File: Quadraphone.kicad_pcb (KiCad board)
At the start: 4 copper layers, 60 x 100 mm, 197 parts, among them J1 Conn_01x10_Male, J2 Conn_01x10_Male, J3 Conn_01x10_Male, J4 Conn_01x10_Male, J5 Eurorack_10_pin_power, Q1 MMBT3904, U1 AMS1117-5.0, U10 TL072, U11 74LV4066PW, U12 SSI2131, U13 TL072, U14 LM4040DBZ-2.5, U15 74LV4066PW, U16 TL072, U17 SSI2131, U18 TL072, U22 SSI2131, U3 MCP6002, U4 LM4040DBZ-5, U5 MCP6004, U6 74LV4066PW, U7 74LV4066PW, U8 74LV4066PW, U9 SSI2131

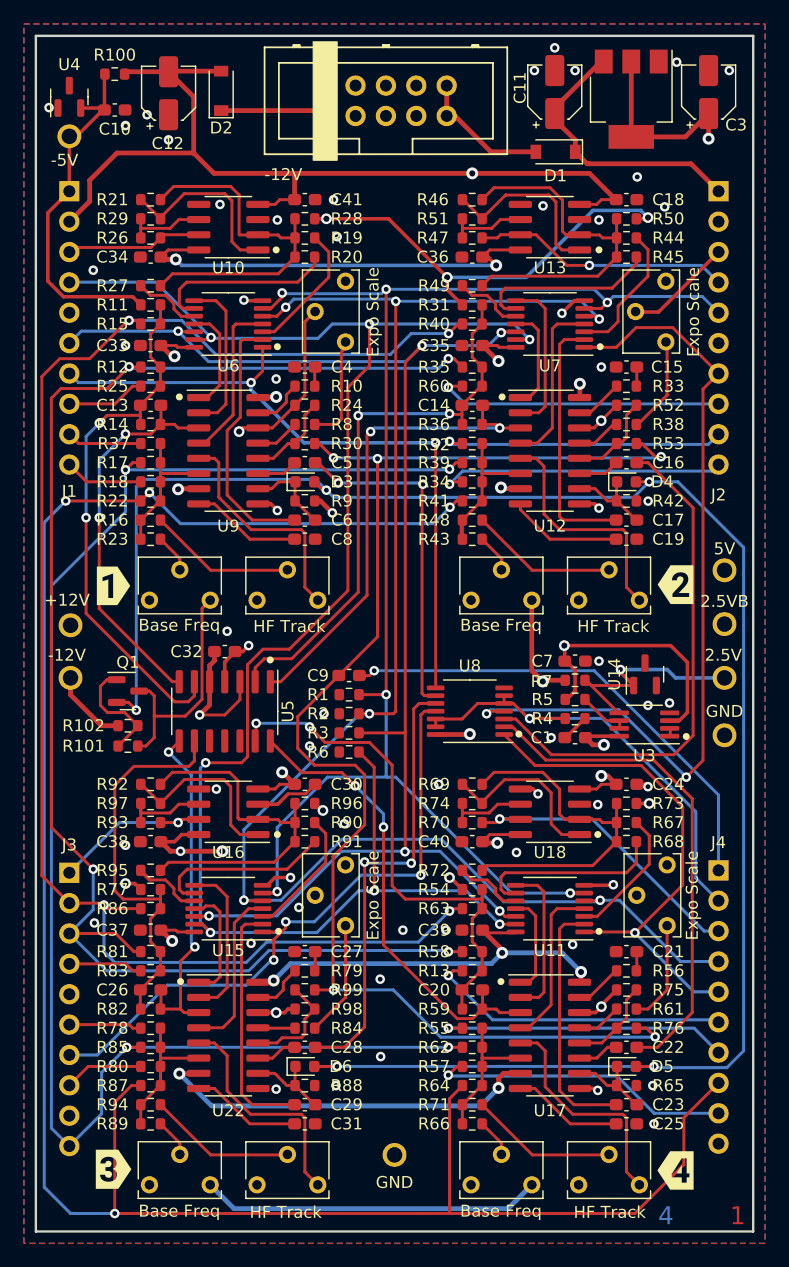
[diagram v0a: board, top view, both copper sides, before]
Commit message: Started Rev 3 with buffered octave control
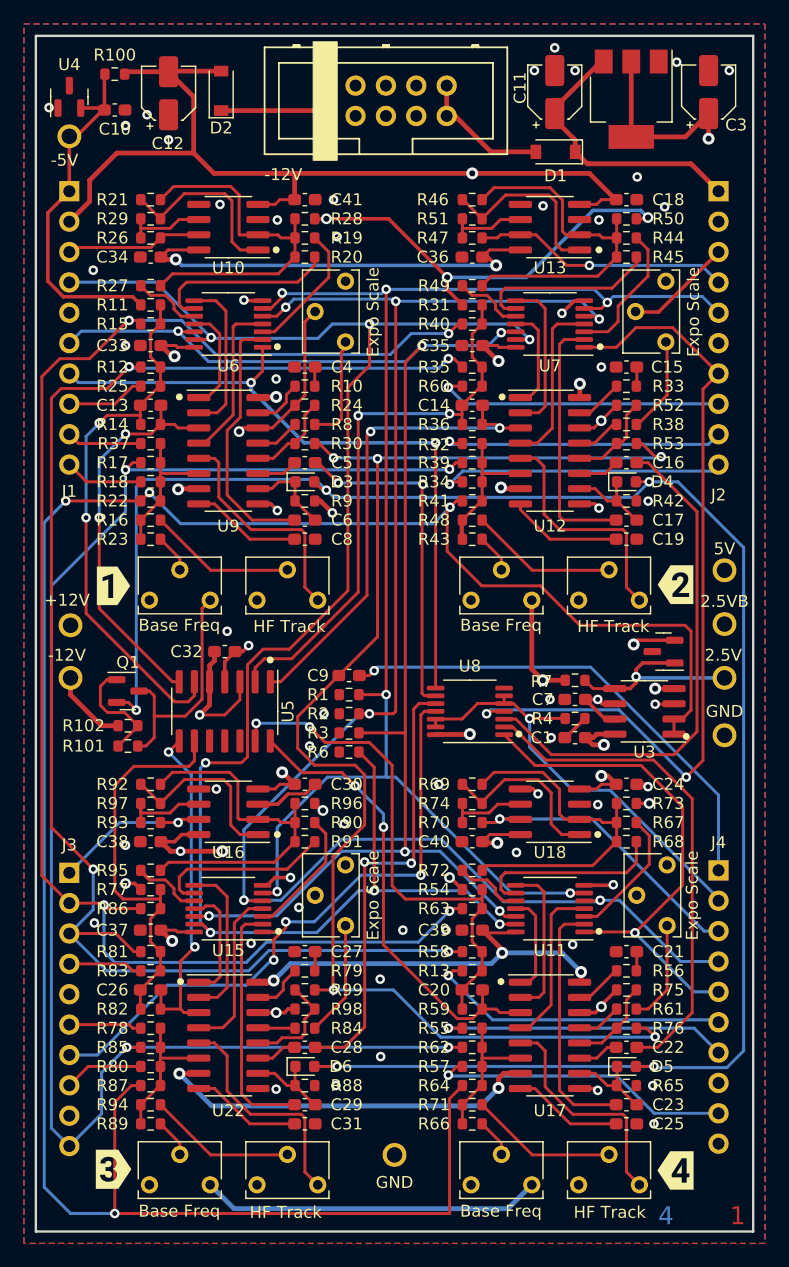
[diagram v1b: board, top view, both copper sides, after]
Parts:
- removed R5: 100, Resistor_SMD:R_0603_1608Metric
- U3: footprint Package_SO:MSOP-8_3x3mm_P0.65mm -> Package_SO:SOIC-8_3.9x4.9mm_P1.27mm
- moved C7 3.20 mm to (95.1, 105.5), turned to 0 degrees
- moved U14 2.45 mm to (102.5, 101.5), turned to 180 degrees
- moved U3 1.10 mm to (100.9, 106.5)
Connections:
- R22 pad 1: /OCT_TUNE -> /Oct_Buff
- R41 pad 1: /OCT_TUNE -> /Oct_Buff
- R64 pad 1: /OCT_TUNE -> /Oct_Buff
- R87 pad 1: /OCT_TUNE -> /Oct_Buff
- U3 pad 1: Net-(U3-Pad1) -> /Oct_Buff
- U3 pad 2: Net-(U3-Pad1) -> /Oct_Buff
- U3 pad 3: +2V5 -> /OCT_TUNE
- U3 pad 6: Net-(R5-Pad1) -> +2V5
- U3 pad 7: Net-(R5-Pad1) -> +2V5
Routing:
- net /Oct_Buff: track 0.00 -> 190.0 mm, vias 0 -> 4
- net /OCT_TUNE: track 183.3 -> 37.3 mm, vias 4 -> 1
- net +2V5: track 294.8 -> 273.1 mm
- net GND: track 37.8 -> 42.9 mm
- net Net-(R5-Pad1): track 4.25 -> 0.00 mm
- net +5V: track 337.1 -> 334.7 mm
- net /2.5V_Test: track 18.8 -> 16.8 mm
- net /SOFT_SYNCH_SW: track 38.6 -> 36.8 mm
- net Net-(U3-Pad1): track 0.65 -> 0.00 mm
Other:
- board text added: "Quadraphone Components v3.0 Mountjoy Modular"
- board text removed: "Quadraphone Components v2.0 Mountjoy Modular"

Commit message: Updates to v3; changed output mix feedback resistors to lower output level
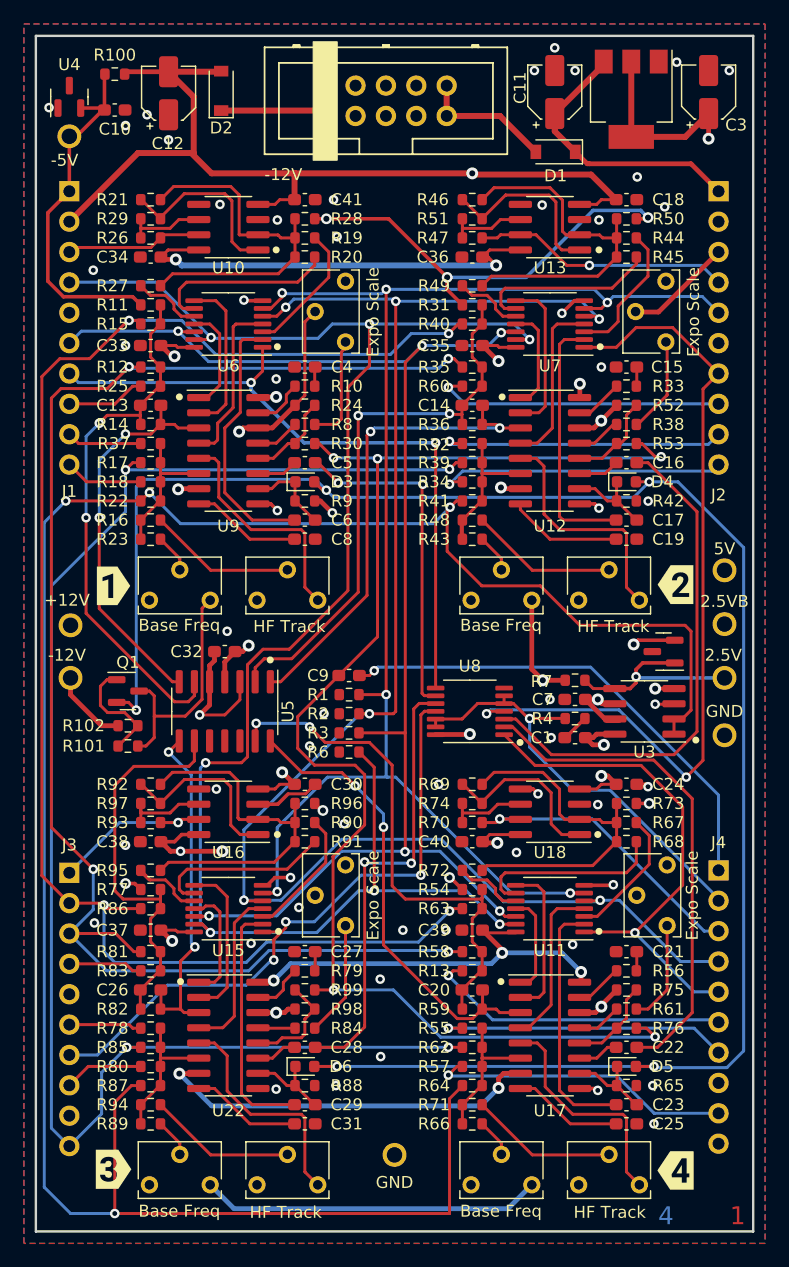
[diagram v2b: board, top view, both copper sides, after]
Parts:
- R1, R2, R3, R4, R6: value 14k -> 13k
- R24, R52, R75, R98: value 499k -> 510k
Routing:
- net -12V: track 284.7 -> 282.6 mm
